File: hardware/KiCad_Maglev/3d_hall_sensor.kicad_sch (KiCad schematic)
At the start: 5 parts, among them U2 TMAG5173A2QDBVRQ1

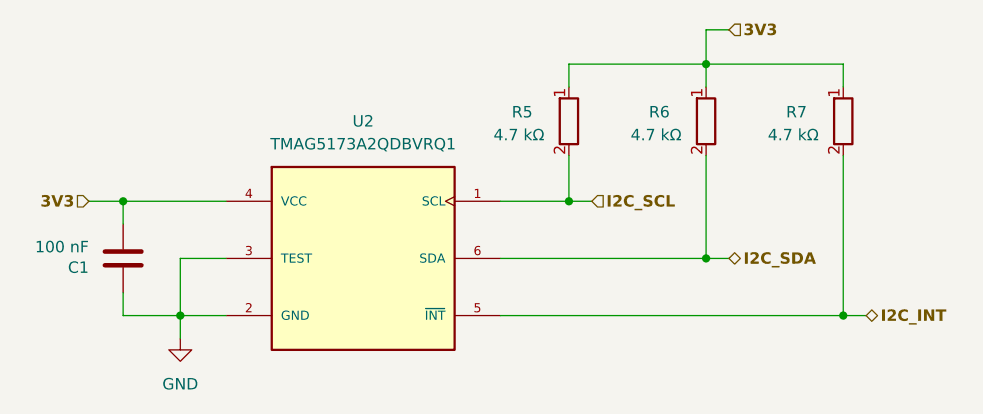
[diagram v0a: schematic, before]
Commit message: Added Footprints/Models for coil and ringmagnet, changed most components to 1206 series
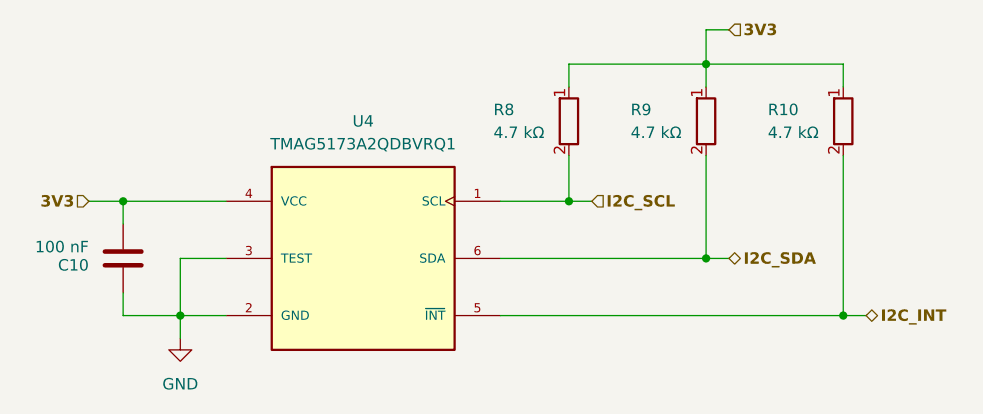
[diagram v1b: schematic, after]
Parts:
- removed C1: 1812_H1.25_885012210008, Capacitor_SMD_Wurth:C_Wurth_WCAP-CSGP-1812_H1.25, symbol Capacitor_Wurth_WCAP-CSGP:1812_H1.25_885012210008
- removed R5, R6, R7: 0603_R_560112116006, Resistor_SMD_Wurth:R_Wurth_WRIS-RSKS-0603_R, symbol Resistor_Wurth_WRIS-RSKS:0603_R_560112116006
- added C10: 1206_H1.25_885012208118, Capacitor_SMD_Wurth:C_Wurth_WCAP-CSGP-1206_H1.25, symbol Capacitor_Wurth_WCAP-CSGP:1206_H1.25_885012208118
- added R10, R8, R9: 1206_R_560112132020, Resistor_SMD_Wurth:R_Wurth_WRIS-RSKS-1206_R, symbol Resistor_Wurth_WRIS-RSKS:1206_R_560112132020
- renumbered U2 to U4
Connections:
- net 3V3: now also C10.1, R10.1, R8.1, R9.1
- net GND: now also C10.2
- net I2C_INT: now also R10.2
- net I2C_SCL: now also R8.2
- net I2C_SDA: now also R9.2

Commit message: Improved power pcb a little and added silkscreen description
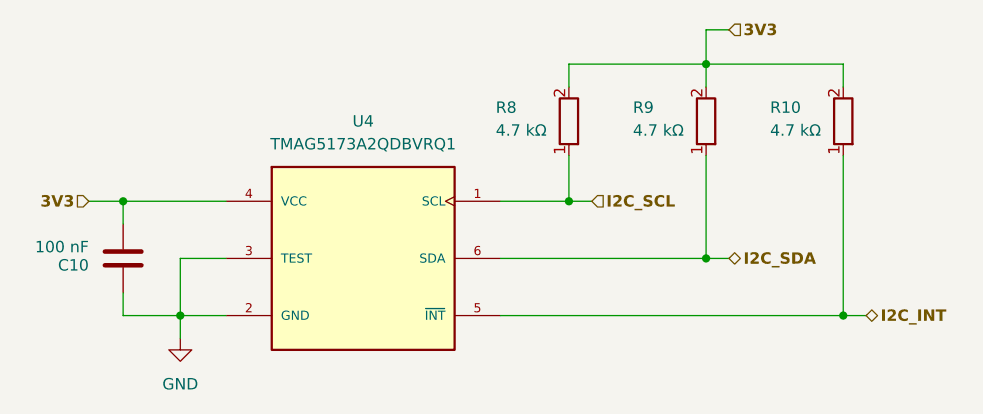
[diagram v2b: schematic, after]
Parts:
- removed R10, R8, R9: 1206_R_560112132020, Resistor_SMD_Wurth:R_Wurth_WRIS-RSKS-1206_R, symbol Resistor_Wurth_WRIS-RSKS:1206_R_560112132020
- added R10, R8, R9: 0805_R_560112120030, Resistor_SMD_Wurth:R_Wurth_WRIS-RSKS-0805_R, symbol Resistor_Wurth_WRIS-RSKS:0805_R_560112120030
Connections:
- net 3V3: now also R10.2, R8.2, R9.2
- net I2C_INT: now also R10.1
- net I2C_SCL: now also R8.1
- net I2C_SDA: now also R9.1
